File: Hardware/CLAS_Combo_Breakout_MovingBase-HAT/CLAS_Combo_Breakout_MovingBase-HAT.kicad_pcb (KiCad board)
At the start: 4 copper layers, 60 x 60 mm, 88 parts, among them J1 USB_C_Receptacle_USB2.0, J2 ZED, J3 NEO, J4 USB_C_Receptacle_USB2.0, J5 Conn_Coaxial, Q1 DSS20200, U1 USBLC6-2P6, U2 ZED-F9P, U3 NEO-D9C-00B, U4 USBLC6-2P6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

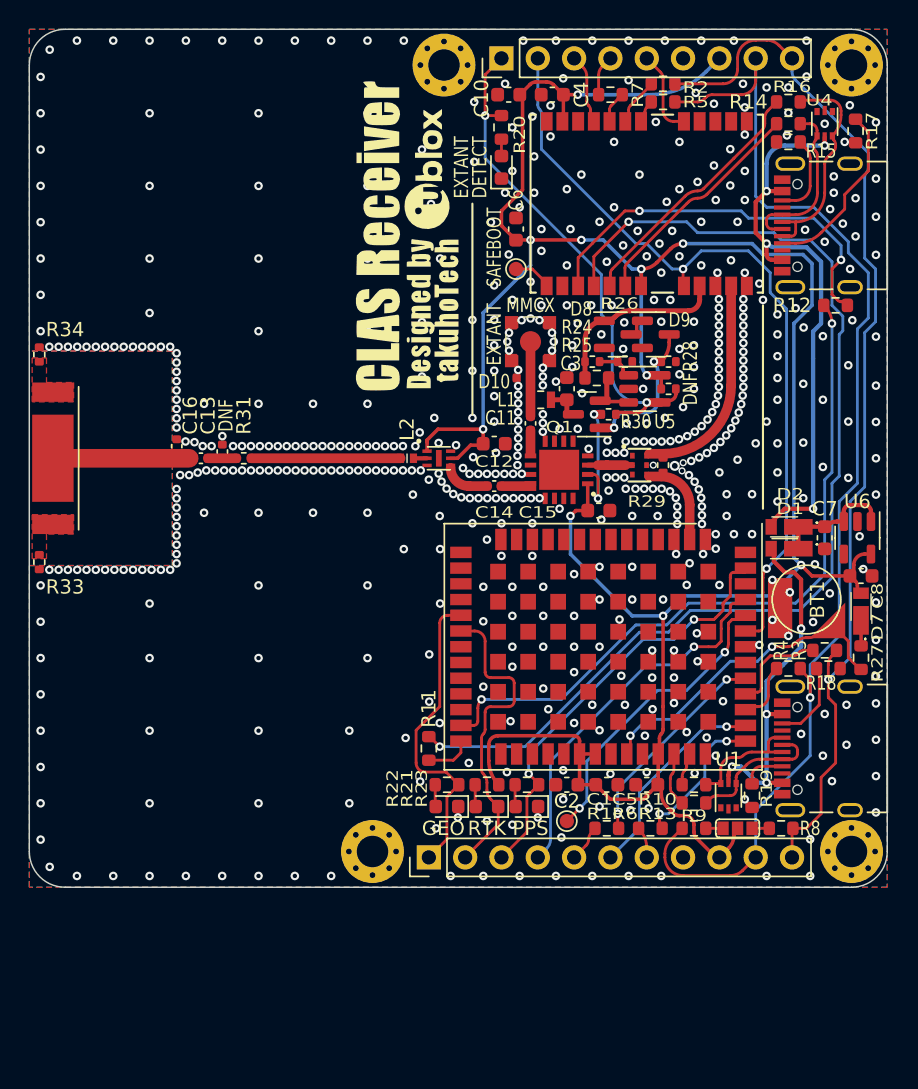
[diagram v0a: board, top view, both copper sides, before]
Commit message: 同軸コネクタのフットプリントを追加
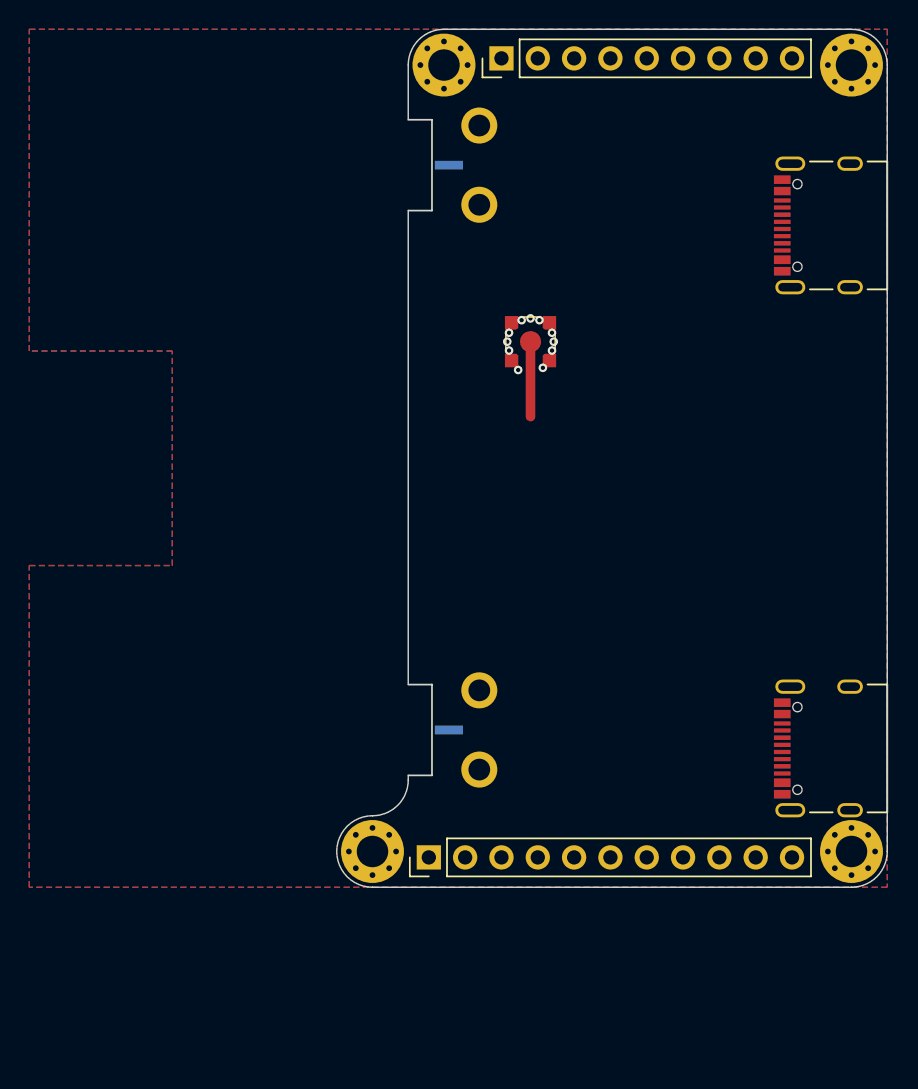
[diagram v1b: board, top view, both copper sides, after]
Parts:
- removed ANT1: GGBLA.125.A, GGBLA.125.A:GGBLA.125.A
- removed BT1: MS421R, Battery_extlib:MS421R
- removed C1, C10, C5, C6, C7, C8: 1u, Capacitor_SMD:C_0603_1608Metric
- removed C11, C14: 47p, Capacitor_SMD:C_0402_1005Metric
- removed C12: 1000p, Capacitor_SMD:C_0603_1608Metric
- removed C13: 3.9p, Capacitor_SMD:C_0402_1005Metric
- removed C15, C2, C3, C4: 0.1u, Capacitor_SMD:C_0603_1608Metric
- removed C16: 1.2p, Capacitor_SMD:C_0402_1005Metric
- removed C9: DNF, Capacitor_SMD:C_0402_1005Metric
- removed D1, D2, D7: CUHS20S30, CUHS20S30:CUHS20S30
- removed D10: PESD0402-140, Diode_SMD:D_0402_1005Metric
- removed D3: EXTANT, LED_SMD:LED_0603_1608Metric
- removed D4: RTK, LED_SMD:LED_0603_1608Metric
- removed D5: GEO, LED_SMD:LED_0603_1608Metric
- removed D6: PPS, LED_SMD:LED_0603_1608Metric
- removed D8: BAS19, Package_TO_SOT_SMD:SOT-23
- removed D9: BAT54W, Package_TO_SOT_SMD:SOT-23
- removed G***: LOGO, LOGO_CLAS_Receiver:CLAS_Receiver
- removed JP1: I2C, Jumper_extlib:SolderJumper-3_Open_RoundedPad
- removed L1: LQW18ANR12G8ZD, LQW18ANR12G8ZD:LQW18ANR12G8ZD
- removed L2: LQW15AN9N5G00D, LQW15AN9N5G00D:LQW15AN9N5G00D
- removed Q1: DSS20200, Package_TO_SOT_SMD:SOT-23
- removed R1, R11, R12, R2, R3, R4, R5, R6, R7: 33, Resistor_SMD:R_0603_1608Metric
- removed R10, R13, R14, R16: 27, Resistor_SMD:R_0603_1608Metric
- removed R15, R17, R18, R19: 5.1k, Resistor_SMD:R_0603_1608Metric
- removed R20, R21, R22, R23: 1k, Resistor_SMD:R_0603_1608Metric
- removed R24: 68, Resistor_SMD:R_0402_1005Metric
- removed R25: 3, Resistor_SMD:R_0603_1608Metric
- removed R26: 22k, Resistor_SMD:R_0402_1005Metric
- removed R27: 3.3k, Resistor_SMD:R_0603_1608Metric
- removed R28: 1.5k, Resistor_SMD:R_0402_1005Metric
- removed R29, R30: 100, Resistor_SMD:R_0402_1005Metric
- removed R31, R33, R34: 0, Resistor_SMD:R_0402_1005Metric
- removed R32: DNF, Resistor_SMD:R_0402_1005Metric
- removed R8, R9: 2.2k, Resistor_SMD:R_0603_1608Metric
- removed TP1: SAFEBOOT_ZED, TestPoint:TestPoint_Pad_D1.0mm
- removed TP2: SAFEBOOT_NEO, TestPoint:TestPoint_Pad_D1.0mm
- removed U1, U4: USBLC6-2P6, Package_TO_SOT_SMD:SOT-666
- removed U2: ZED-F9P, RF_GPS:ublox_ZED
- removed U3: NEO-D9C-00B, NEO-D9:NEO-D9
- removed U5: NJU77251F, Package_TO_SOT_SMD:SOT-23-5
- removed U6: AP2112K-3.3, Package_TO_SOT_SMD:SOT-23-5
- removed U7: NT1191GEAE3S, NT1191GEAE3S:NT1191GEAE3S
- removed U8: F2933NBGP, F2933NBGP:F2933NBGP
- removed U9: PD0922J5050S2HF, PD0922J5050S2HF:PD0922J5050S2HF_ANA
- added REF**: 0732512440, Connector_Coaxial_extlib:SMA_Molex_0732512440_embed, B.Cu at (126.5, 99.5)
- added REF**: 0732512440, Connector_Coaxial_extlib:SMA_Molex_0732512440_embed_DL868-915M-R-48_0deg, B.Cu at (126.5, 139.0)
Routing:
- net +3.3V: track 182.7 -> 0.00 mm, vias 10 -> 0
- net /SDA: track 84.5 -> 0.00 mm, vias 1 -> 0
- net Net-(R11-Pad2): track 77.0 -> 0.00 mm, vias 2 -> 0
- net /SCL: track 74.7 -> 0.00 mm, vias 1 -> 0
- net /RESET: track 55.5 -> 0.00 mm, vias 2 -> 0
- net Net-(R12-Pad1): track 49.7 -> 0.00 mm, vias 2 -> 0
- net /VBUS_NEO: track 40.1 -> 0.00 mm, vias 4 -> 0
- net /EXTANT_DETECT: track 36.3 -> 0.00 mm, vias 2 -> 0
- net /TP: track 30.5 -> 0.00 mm, vias 2 -> 0
- net Net-(R12-Pad2): track 27.9 -> 0.00 mm, vias 2 -> 0
- net /EXTINT_ZED: track 26.6 -> 0.00 mm, vias 1 -> 0
- net /VBUS_ZED: track 25.0 -> 0.00 mm, vias 4 -> 0
- net /V_BACKUP: track 22.4 -> 0.00 mm, vias 2 -> 0
- net /RTK: track 21.9 -> 0.00 mm
- net /GEO: track 21.9 -> 0.00 mm
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- removed copper zone on F.Cu, net Net-(ANT1-Pad2)
- removed copper zone on F.Cu, net Net-(ANT1-Pad3)
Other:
- board size 60 x 60 mm -> 38.5 x 60 mm
- board text added: "LNAの中心"
- board text removed: "DETECT"
- board text removed: "DNF"
- board text removed: "SAFEBOOT"
- board text removed: "外周にビアを置くときは、基板中心を原点にする"

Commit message: E220-900T22S(JP)のフットプリントを追加修整
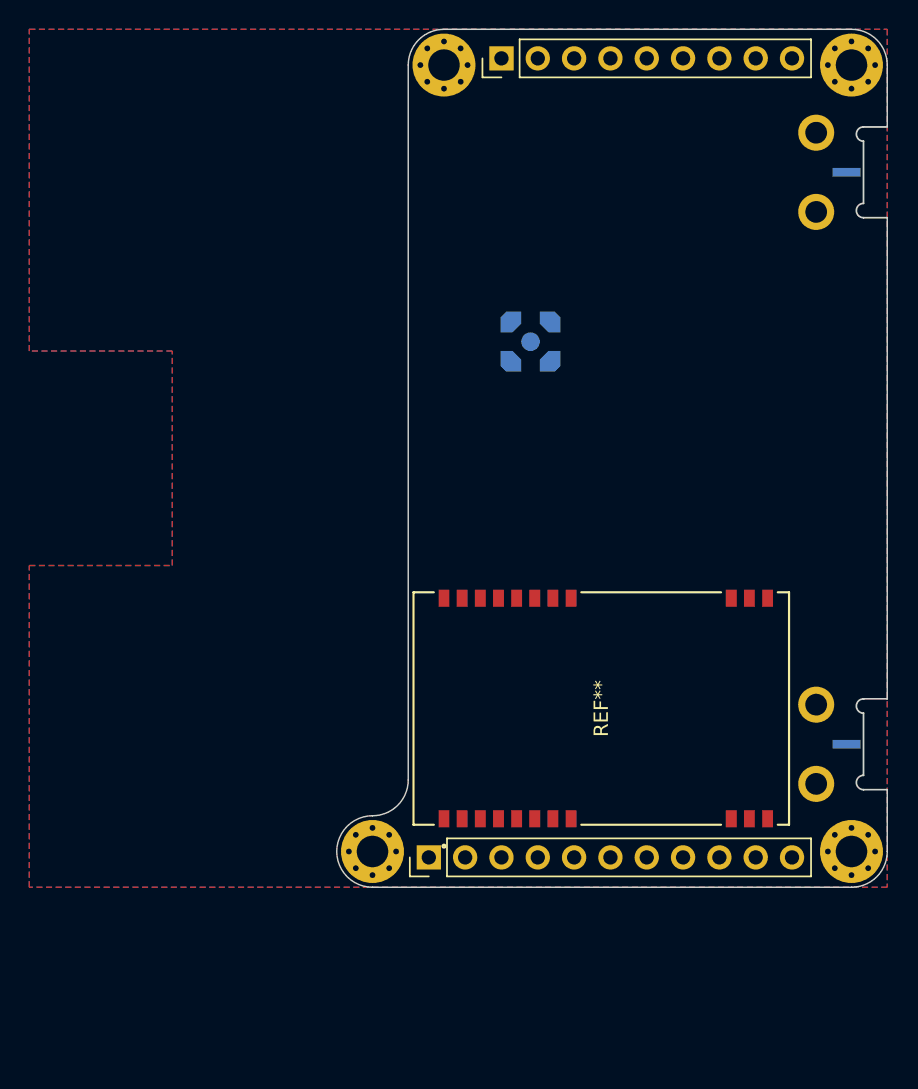
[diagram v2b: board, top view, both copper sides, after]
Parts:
- removed J1, J4: USB_C_Receptacle_USB2.0, Connector_USB_extlib:USB_C_Receptacle_5077CR-16-SMC2-BK-TR
- removed J5: Conn_Coaxial, Connector_Coaxial_extlib:0734152063
- removed the REF** at (126.5, 139.0)
- added J**: 0734152063, Connector_Coaxial_extlib:MMCX_Samtec_MMCX-P-P-H-ST-SM1_Male, B.Cu at (135.1, 111.8)
- added REF**: E220-900T22S_BYT, RF_Module_extlib:E220-900T22S(JP), F.Cu at (140.0, 137.5)
- added REF**: 0732512440, Connector_Coaxial_extlib:SMA_Molex_0732512440_embed_DL868-915M-R-48_180deg, B.Cu at (160.0, 140.0)
- moved REF** 33.5 mm to (160.0, 100.0), turned to 180 degrees
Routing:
- net Net-(C11-Pad1): track 5.23 -> 0.00 mm
- net GND: vias 11 -> 0
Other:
- outline, holes or cut-outs redrawn

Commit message: ISP4520のフットプリントを追加編集
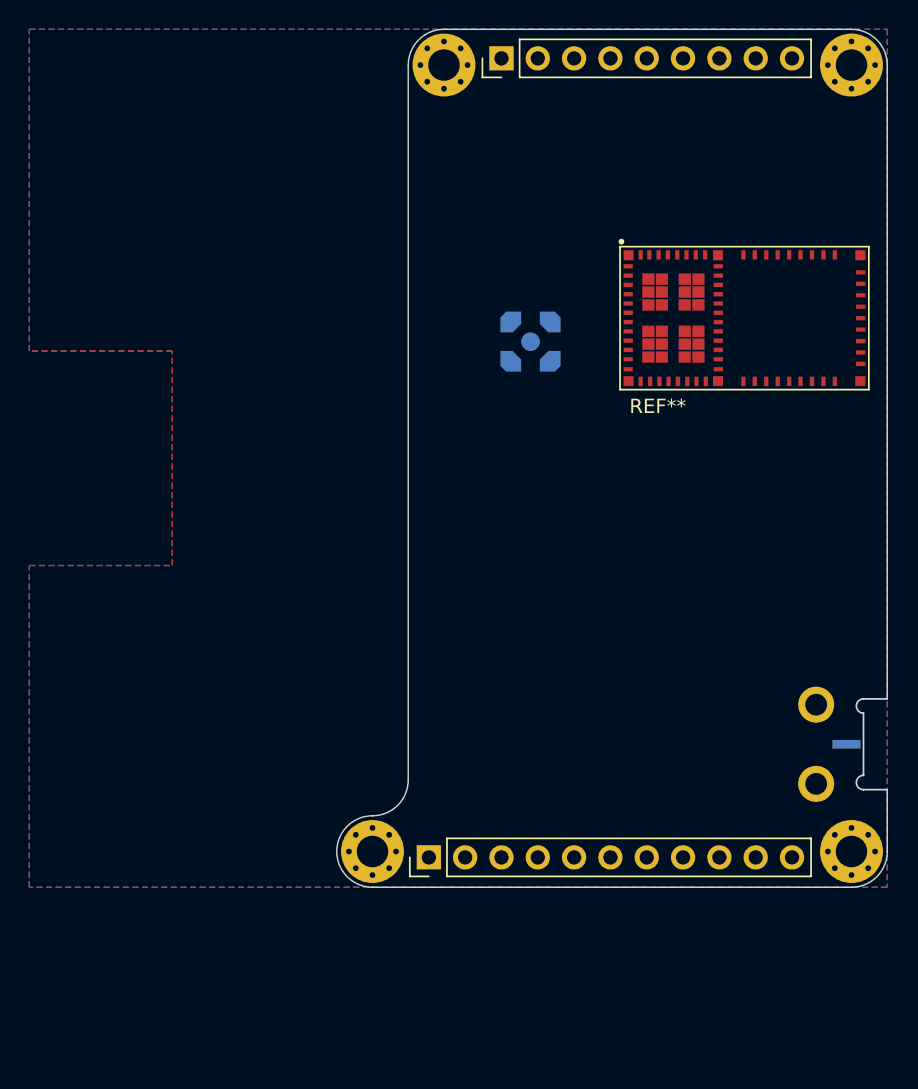
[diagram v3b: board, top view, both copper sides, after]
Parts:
- removed the REF** at (140.0, 137.5)
- removed the REF** at (160.0, 140.0)
- added REF**: ISP4520-AS, RF_Module_extlib:ISP4520-AS, F.Cu at (141.4, 115.1)
- moved REF** 40.0 mm to (160.0, 140.0)
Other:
- outline, holes or cut-outs redrawn
- board text added: "ボード間距離は8.0mm"

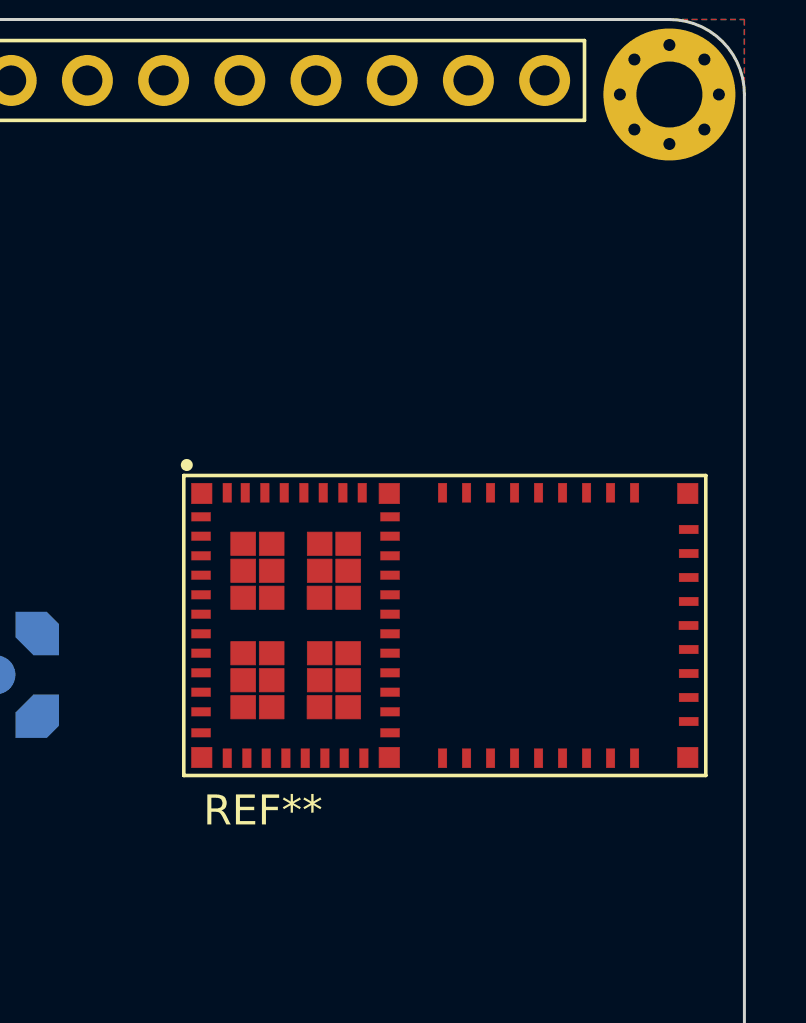
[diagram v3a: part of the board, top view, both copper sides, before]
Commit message: 電源回路描いた
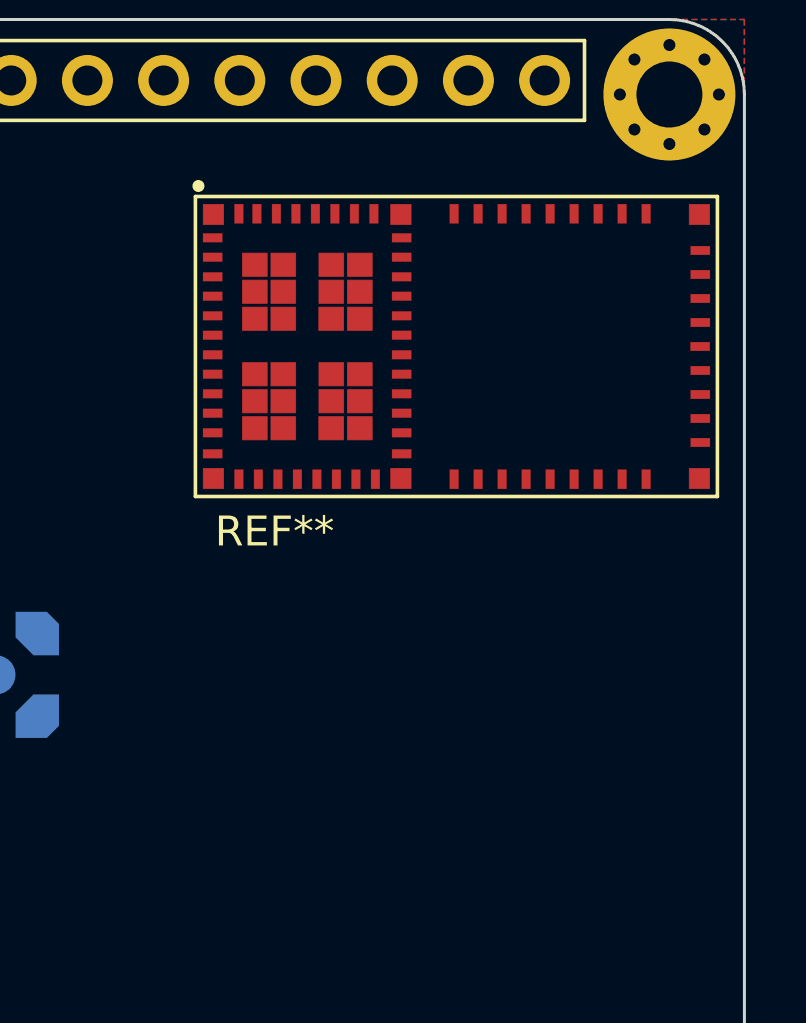
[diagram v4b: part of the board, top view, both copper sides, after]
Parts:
- moved REF** 26.0 mm to (159.0, 96.0)
